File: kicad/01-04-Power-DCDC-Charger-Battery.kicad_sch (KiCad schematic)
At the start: 49 parts, among them J3 S2B-PH-K-S_LF__SN_, Q1 PMOS, Q2 AO3400A, Q3 AO3400A, U2 BQ29700DSER, U3 MCP73831-2-OT, U4 TLV62568DBV

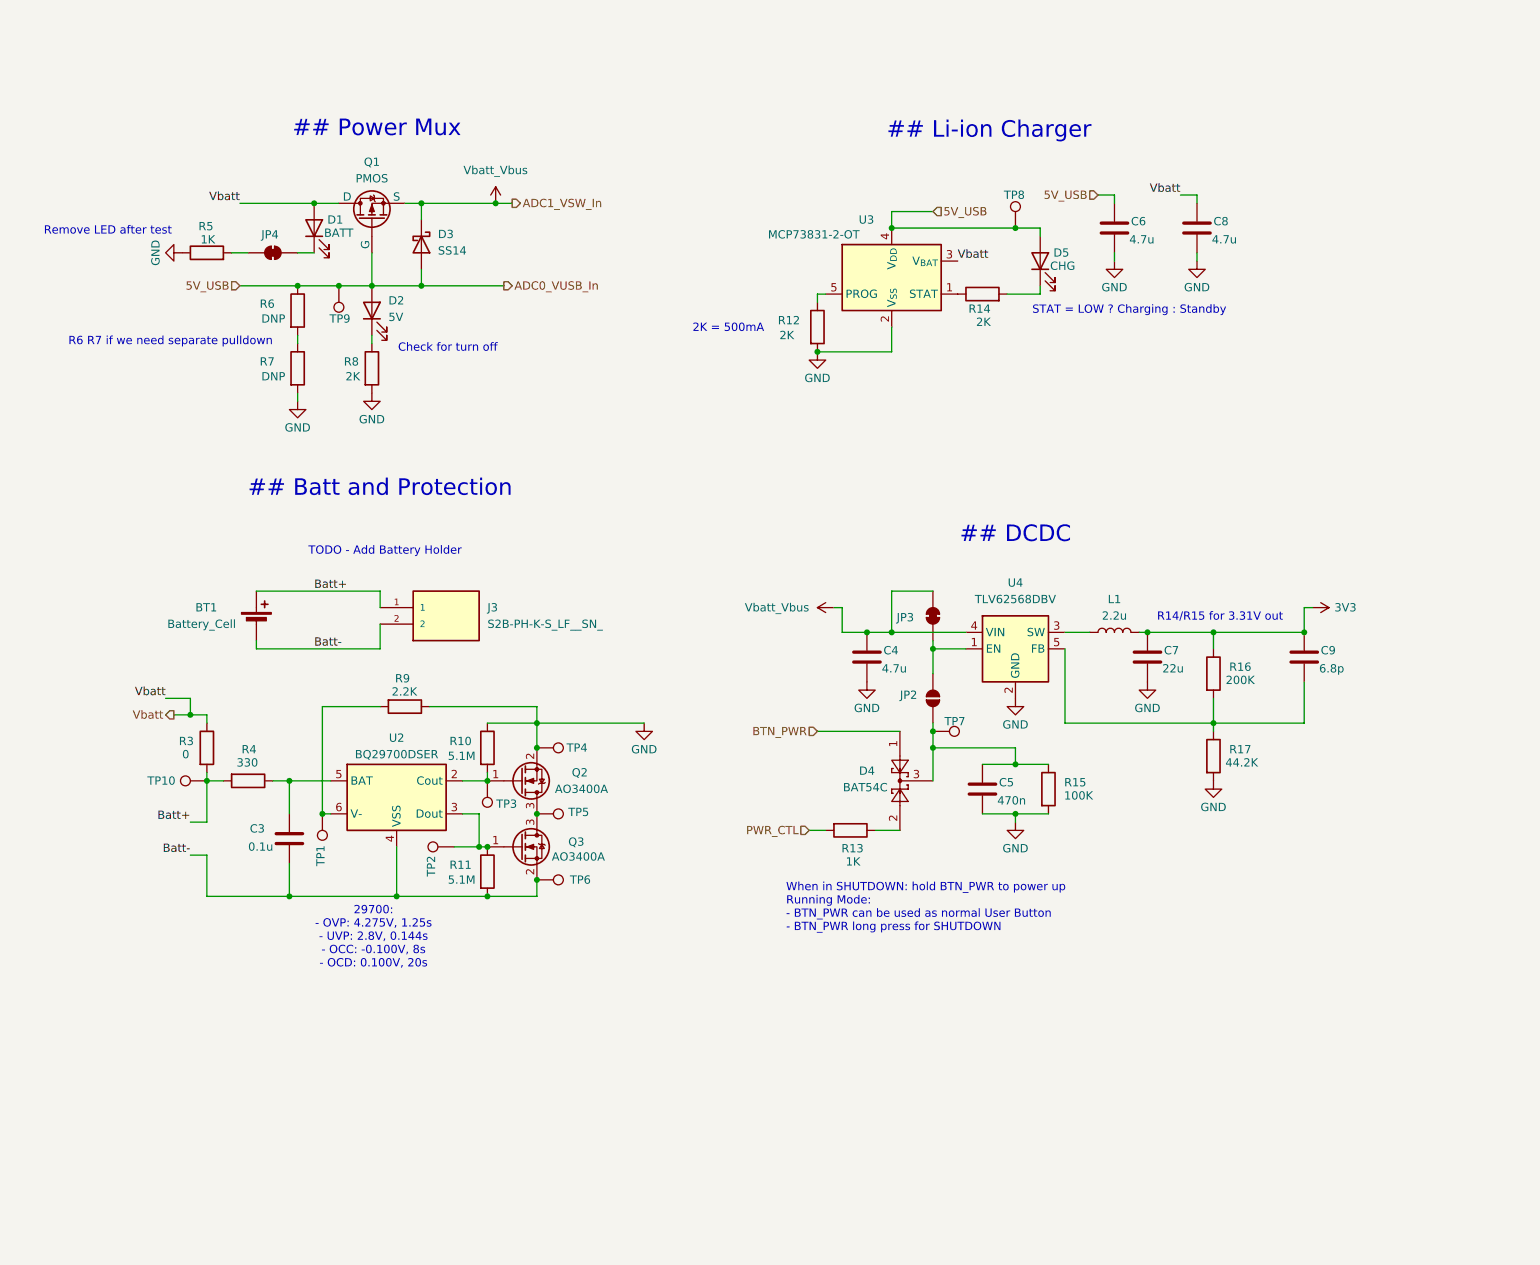
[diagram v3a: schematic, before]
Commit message: DR  ✅ SYS-01-Power-Mux
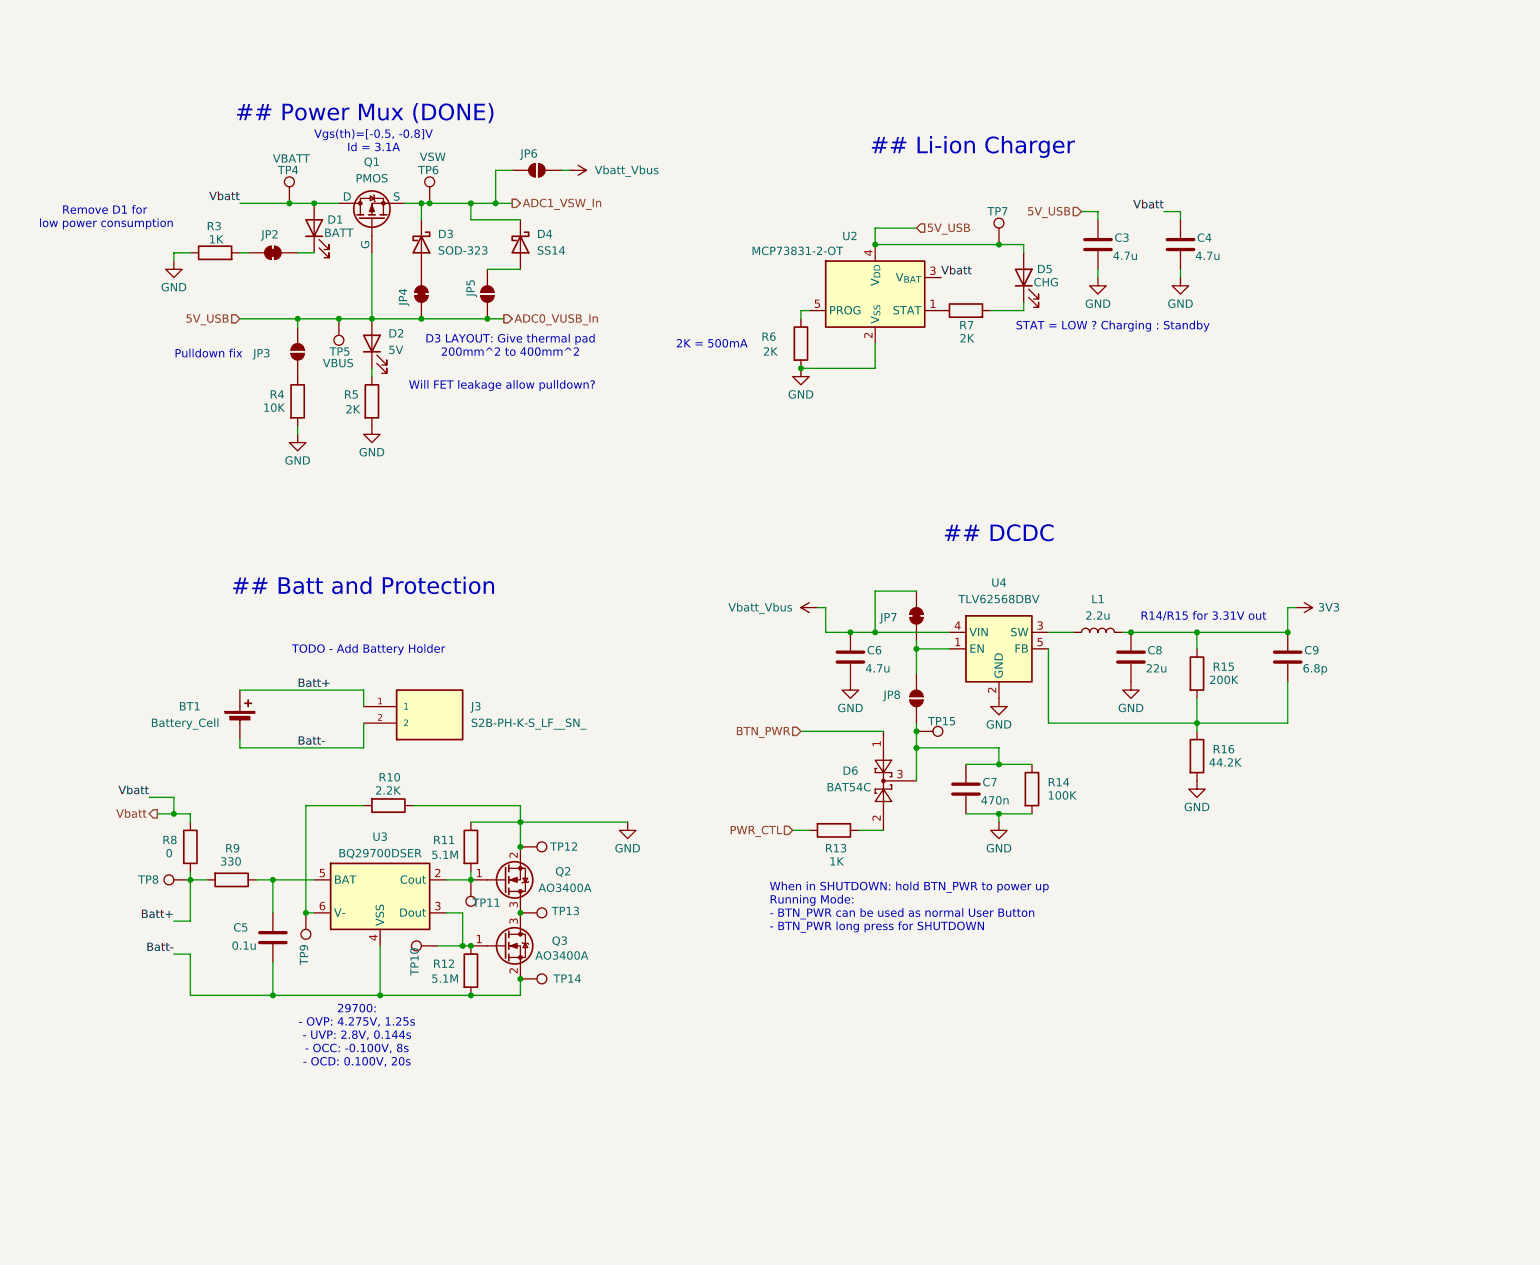
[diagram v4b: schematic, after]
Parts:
- removed R6, R7: DNP, symbol Device:R
- added D4: SS14, Diode_SMD:D_SMA, symbol Diode:SS14
- added JP3, JP5, JP6: SolderJumper_2_Open, Jumper:SolderJumper-2_P1.3mm_Open_RoundedPad1.0x1.5mm, symbol Jumper:SolderJumper_2_Open
- added JP4: SolderJumper_2_Bridged, Jumper:SolderJumper-2_P1.3mm_Bridged_RoundedPad1.0x1.5mm, symbol Jumper:SolderJumper_2_Bridged
- added R4: 10K, Resistor_SMD:R_0805_2012Metric_Pad1.20x1.40mm_HandSolder, symbol Device:R
- added TP4: VBATT, project footprints:TestPoint_THTPad_D2.0mm_Drill1.0mm, symbol Connector:TestPoint
- added TP6: VSW, project footprints:TestPoint_THTPad_D2.0mm_Drill1.0mm, symbol Connector:TestPoint
- D1, D2, Q1: Subsystem (none) -> 01-Power-Mux
- D3: value SS14 -> SOD-323; footprint Diode_SMD:D_SMA -> Diode_SMD:D_SOD-323_HandSoldering; MPN (none) -> PMEG1020EA,115; Manufacturer (none) -> Nexperia; Package (none) -> SOD-323; Subsystem (none) -> 01-Power-Mux; Supplier 1 (none) -> LCSC; Supplier 1 SKU (none) -> C426863; Supplier 1 URL (none) -> https://lcsc.com/product-detail/Schottky-Diodes_Nexperia-PM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
- JP2: renamed from JP4; footprint (none) -> Jumper:SolderJumper-2_P1.3mm_Bridged_RoundedPad1.0x1.5mm; Subsystem (none) -> 01-Power-Mux
- JP7: renamed from JP3; footprint (none) -> Jumper:SolderJumper-2_P1.3mm_Bridged_RoundedPad1.0x1.5mm
- JP8: renamed from JP2; footprint (none) -> Jumper:SolderJumper-2_P1.3mm_Open_RoundedPad1.0x1.5mm
- R10: renamed from R9; footprint (none) -> Resistor_SMD:R_0805_2012Metric_Pad1.20x1.40mm_HandSolder
- R11: renamed from R10; footprint (none) -> Resistor_SMD:R_0805_2012Metric_Pad1.20x1.40mm_HandSolder
- R12: renamed from R11; footprint (none) -> Resistor_SMD:R_0805_2012Metric_Pad1.20x1.40mm_HandSolder
- R13: footprint (none) -> Resistor_SMD:R_0805_2012Metric_Pad1.20x1.40mm_HandSolder
- R14: renamed from R15; footprint (none) -> Resistor_SMD:R_0805_2012Metric_Pad1.20x1.40mm_HandSolder
- R15: renamed from R16; footprint (none) -> Resistor_SMD:R_0805_2012Metric_Pad1.20x1.40mm_HandSolder
- R16: renamed from R17; footprint (none) -> Resistor_SMD:R_0805_2012Metric_Pad1.20x1.40mm_HandSolder
- R3: renamed from R5; footprint (none) -> Resistor_SMD:R_0805_2012Metric_Pad1.20x1.40mm_HandSolder
- R5: renamed from R8; footprint (none) -> Resistor_SMD:R_0805_2012Metric_Pad1.20x1.40mm_HandSolder; Subsystem (none) -> 01-Power-Mux
- R6: renamed from R12; footprint (none) -> Resistor_SMD:R_0805_2012Metric_Pad1.20x1.40mm_HandSolder
- R7: renamed from R14; footprint (none) -> Resistor_SMD:R_0805_2012Metric_Pad1.20x1.40mm_HandSolder
- R8: renamed from R3; footprint (none) -> Resistor_SMD:R_0805_2012Metric_Pad1.20x1.40mm_HandSolder
- R9: renamed from R4; footprint (none) -> Resistor_SMD:R_0805_2012Metric_Pad1.20x1.40mm_HandSolder
- TP10: renamed from TP2; footprint (none) -> project footprints:TestPoint_THTPad_D2.0mm_Drill1.0mm
- TP11: renamed from TP3; footprint (none) -> project footprints:TestPoint_THTPad_D2.0mm_Drill1.0mm
- TP12: renamed from TP4; footprint (none) -> project footprints:TestPoint_THTPad_D2.0mm_Drill1.0mm
- TP13: renamed from TP5; footprint (none) -> project footprints:TestPoint_THTPad_D2.0mm_Drill1.0mm
- TP14: renamed from TP6; footprint (none) -> project footprints:TestPoint_THTPad_D2.0mm_Drill1.0mm
- TP15: renamed from TP7; footprint (none) -> project footprints:TestPoint_THTPad_D2.0mm_Drill1.0mm
- TP5: renamed from TP9; value TestPoint -> VBUS; footprint (none) -> project footprints:TestPoint_THTPad_D2.0mm_Drill1.0mm; Subsystem (none) -> 01-Power-Mux
- TP7: renamed from TP8; footprint (none) -> project footprints:TestPoint_THTPad_D2.0mm_Drill1.0mm
- TP8: renamed from TP10; footprint (none) -> project footprints:TestPoint_THTPad_D2.0mm_Drill1.0mm
- TP9: renamed from TP1; footprint (none) -> project footprints:TestPoint_THTPad_D2.0mm_Drill1.0mm
- renumbered C6 to C3, C8 to C4, C3 to C5, C4 to C6, C5 to C7, C7 to C8, D4 to D6, U3 to U2, U2 to U3
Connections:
- net 5V_USB: now also JP3.2 (B), JP4.2 (B), JP5.1 (A); no longer D3.2 (A)
- net GND: now also R4.2
- net Vbatt: now also TP4.1
- net Vbatt_Vbus: now also JP6.1 (A); no longer D3.1 (K), Q1.3 (S)
- new net: D3.2 (A), JP4.1 (A)
- new net: D4.2 (A), JP5.2 (B)
- new net: JP3.1 (A), R4.1
- new net ADC1_VSW_In: D3.1 (K), D4.1 (K), JP6.2 (B), Q1.3 (S), TP6.1
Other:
- note added: "## Power Mux (DONE)"
- note added: "D3 LAYOUT: Give thermal pad 200mm^2 to 400mm^2"
- note added: "Pulldown fix"
- note added: "Remove D1 for low power consumption"
- note added: "Vgs(th)=[-0.5, -0.8]V Id = 3.1A"
- note added: "Will FET leakage allow pulldown?"
- note removed: "## Power Mux"
- note removed: "Check for turn off"
- note removed: "R6 R7 if we need separate pulldown"
- note removed: "Remove LED after test"
- moved on the sheet: BT1, C3, C4, C5, C6, C7, C8, C9, D2, D5, D6, J3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

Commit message: DR SYS-02-DCDC ✅
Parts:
- added D7: 3V3, LED_SMD:LED_0805_2012Metric, symbol Device:LED
- added JP9: SolderJumper_2_Bridged, Jumper:SolderJumper-2_P1.3mm_Bridged_RoundedPad1.0x1.5mm, symbol Jumper:SolderJumper_2_Bridged
- added R17: 1K, Resistor_SMD:R_0805_2012Metric_Pad1.20x1.40mm_HandSolder, symbol Device:R
- added TP16: DC_SW, project footprints:TestPoint_THTPad_D2.0mm_Drill1.0mm, symbol Connector:TestPoint
- C6: footprint (none) -> Capacitor_SMD:C_0603_1608Metric_Pad1.08x0.95mm_HandSolder; MPN (none) -> CL10A475KO8NNNC; Manufacturer (none) -> Samsung Electro-mechanics; Package (none) -> 0603; Subsystem (none) -> 02-DCDC; Supplier 1 (none) -> LCSC; Supplier 1 SKU (none) -> C19666; Supplier 1 URL (none) -> https://jlcpcb.com/partdetail/20375-CL10A475KO8NNNC/C19666
- C7: footprint (none) -> Capacitor_SMD:C_0603_1608Metric_Pad1.08x0.95mm_HandSolder; MPN (none) -> (Generic); Manufacturer (none) -> (Generic); Package (none) -> 0603; Subsystem (none) -> 02-DCDC; Supplier 1 (none) -> (Generic)
- C8: footprint (none) -> Capacitor_SMD:C_0603_1608Metric_Pad1.08x0.95mm_HandSolder; MPN (none) -> CL10A226MQ8NRNC; Manufacturer (none) -> Samsung Electro-Mechanics; Package (none) -> 0603; Subsystem (none) -> 02-DCDC; Supplier 1 (none) -> LCSC; Supplier 1 SKU (none) -> C59461; Supplier 1 URL (none) -> https://jlcpcb.com/partdetail/60514-CL10A226MQ8NRNC/C59461
- C9: MPN (none) -> (Generic); Manufacturer (none) -> (Generic); Package (none) -> 0603; Subsystem (none) -> 02-DCDC; Supplier 1 (none) -> (Generic)
- D6: MPN (none) -> BAT54CLT1G; Manufacturer (none) -> onsemi; Package (none) -> SOT-23; Subsystem (none) -> 02-DCDC; Supplier 1 (none) -> LCSC; Supplier 1 SKU (none) -> C14308; Supplier 1 URL (none) -> https://jlcpcb.com/partdetail/onsemi-BAT54CLT1G/C14308
- JP2, JP3, JP4, JP5, JP6, JP7, JP8, TP10, TP11, TP12, TP13, TP14, TP4, TP5, TP6, TP7, TP8, TP9: MPN (none) -> (Embedded)
- L1: Subsystem (none) -> 02-DCDC
- R13, R14, R15, R16: MPN (none) -> (Generic); Manufacturer (none) -> (Generic); Subsystem (none) -> 02-DCDC; Supplier 1 (none) -> (Generic)
- R4, R5: MPN (none) -> (Generic)
- TP15: value TestPoint -> EN_CTL; MPN (none) -> (Embedded)
- U4: value TLV62568DBV -> TLV62568DBVR; MPN (none) -> TLV62568DBVR; Manufacturer (none) -> Texas Instruments; Package (none) -> SOT23-5; Subsystem (none) -> 02-DCDC; Supplier 1 (none) -> Digikey; Supplier 1 URL (none) -> https://www.digikey.jp/en/products/detail/texas-instruments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
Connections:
- net 3V3: now also JP9.2 (B)
- net GND: now also R17.2
- net DC_FB: now reaches C9.2, R15.2, R16.1, U4.5 (FB)
- net DC_EN_CTL: now reaches C7.1, D6.3, JP8.1 (A), R14.1, TP15.1
- net at L1.1, U4.3 (SW): now also TP16.1
- new net: D7.1 (K), R17.1
- new net: D7.2 (A), JP9.1 (A)
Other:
- note added: "## DCDC (DONE)"
- note added: "R15/R16 for 3.31V out"
- note added: "See Datasheet for layout guidelines -- Must follow for DCDC"
- note removed: "## DCDC"
- note removed: "R14/R15 for 3.31V out"
- moved on the sheet: BT1, C5, C6, C7, C8, C9, D6, J3, JP7, JP8, L1, Q2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

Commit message: DR SYS-03 Charger ✅
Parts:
- added D9: GRN/DONE, LED_SMD:LED_0805_2012Metric, symbol Device:LED
- added JP18, JP19: SolderJumper_2_Bridged, Jumper:SolderJumper-2_P1.3mm_Bridged_RoundedPad1.0x1.5mm, symbol Jumper:SolderJumper_2_Bridged
- added R39: 2K, Resistor_SMD:R_0805_2012Metric_Pad1.20x1.40mm_HandSolder, symbol Device:R
- C3, C4: footprint (none) -> Capacitor_SMD:C_0805_2012Metric_Pad1.18x1.45mm_HandSolder; MPN (none) -> (Generic); Manufacturer (none) -> (Generic); Package (none) -> 0805; Subsystem (none) -> 03-Charger; Supplier 1 (none) -> (Generic)
- D5: value CHG -> RED/CHG; MPN KT-0805G -> NCD0805R1; Manufacturer Hubei KENTO Elec -> Foshan NationStar Optoelectronics; Notes (none) -> JLCPCBA Basic; Subsystem (none) -> 03-Charger; Supplier 1 SKU C2297 -> C84256; Supplier 1 URL https://lcsc.com/product-detail/LED-Indication-Discrete_Hub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 -> https://lcsc.com/product-detail/Light-Emitting-Diodes-LED_F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
- R17: value 1K -> 2K
- R6: value 2K -> 3K; MPN (none) -> (Generic); Manufacturer (none) -> (Generic); Package (none) -> 0805; Subsystem (none) -> 03-Charger; Supplier 1 (none) -> (Generic)
- R7: MPN (none) -> (Generic); Manufacturer (none) -> (Generic); Package (none) -> 0805; Subsystem (none) -> 03-Charger; Supplier 1 (none) -> (Generic)
- TP7: value TestPoint -> STAT
- U2: MPN ABS06-32.768KHZ-9-T -> MCP73831T-2ACI/OT; Manufacturer Abracon LLC -> Microchip Technology; Package SMD2012-2P -> SOT23-5; Subsystem (none) -> 03-Charger; Supplier 1 LSCS -> Digikey; Supplier 1 SKU C1985410 -> (none); Supplier 1 URL https://lcsc.com/product-detail/crystals_abracon-llc-abs06-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 -> https://www.digikey.jp/en/products/detail/microchip-technol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
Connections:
- net 5V_USB: now also JP19.2 (B); no longer D5.2 (A), TP7.1
- net GND: now also D9.1 (K)
- net STAT: now reaches R7.1, U2.1 (STAT)
- net STAT: now also TP7.1, JP18.2 (B)
- new net: D9.2 (A), R39.1
- new net: D5.2 (A), JP19.1 (A)
- new net: JP18.1 (A), R39.2
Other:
- note added: "## Li-ion Charger (D"
- note added: "500mA max I = 1/Rprog"
- note added: "Layout: Give SOT23 large copper pour for heat dissipation"
- note added: "TODO _ DFT _ Test without in loop?"
- note removed: "## Li-ion Charger"
- note removed: "2K = 500mA"
- moved on the sheet: C3, C4, R7, TP7
